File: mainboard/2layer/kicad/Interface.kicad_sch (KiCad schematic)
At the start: 61 parts, among them J1 Conn_02x10_Odd_Even_MountingP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, J21 Conn_01x01_Male, J22 Conn_01x01_Male, J3 DIN-5, J4 DIN-5, J6 Conn_01x10, P11 1N4148, P12 1N4148, P13 1N4148, P14 1N4148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

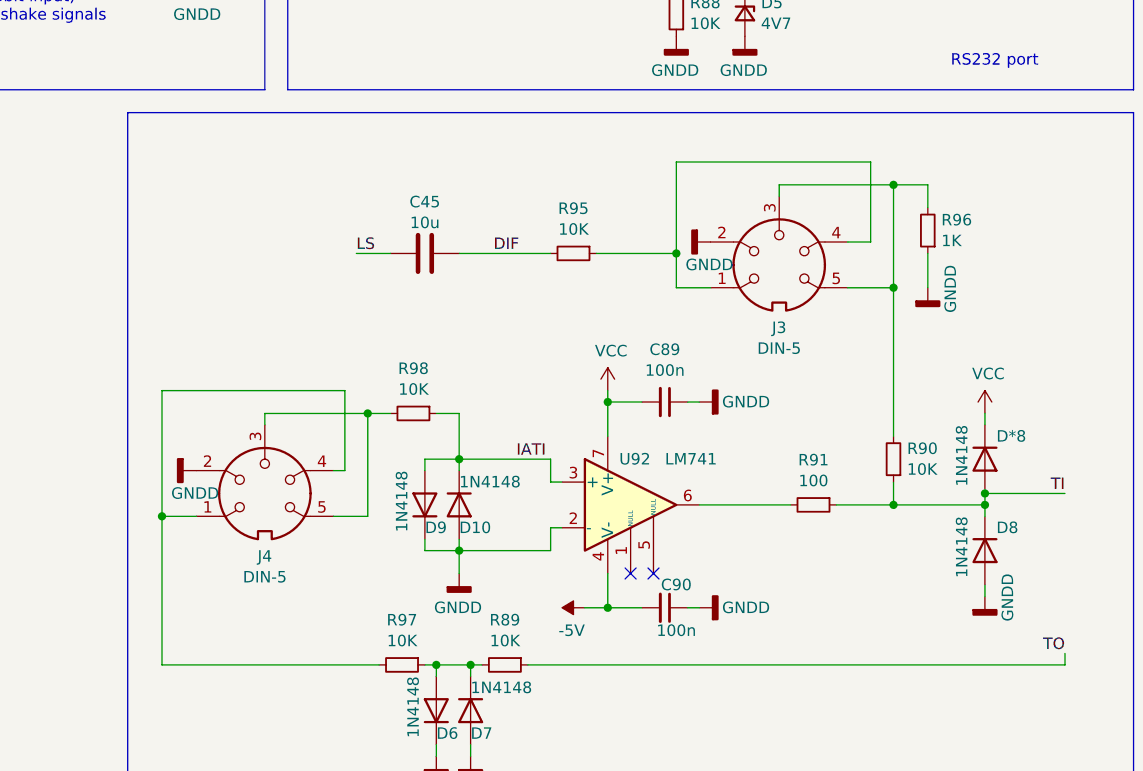
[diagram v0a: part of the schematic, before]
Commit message: Fixes for PCB DRC: trace clearance, footprints, board edges
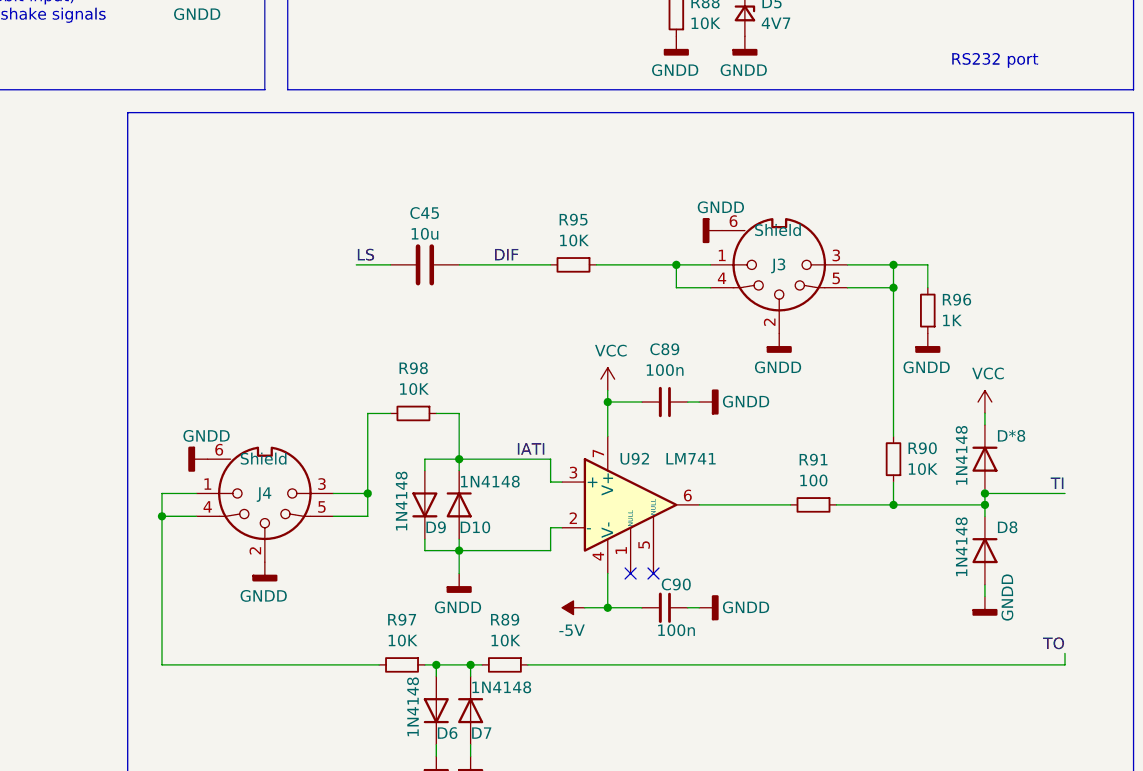
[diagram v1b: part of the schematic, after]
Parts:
- removed J3: DIN-5, Connectors_UNITRA:DIN-5, symbol Connector:DIN-5
- removed J4: DIN-5, Conectors_Unitra:DIN-5, symbol Connector:DIN-5
- added J3, J4: DIN-5, Cobra_original:DIN-5, symbol Connector:DIN-5_180degree_GND
- D*8, D10, D5, D6, D7, D8, D9, P11, P12, P13, P14, P15, P16, P17, P18: footprint Diode_THT:D_DO-35_SOD27_P7.62mm_Horizontal -> Cobra_original:D_DO-35_SOD27_P7.62mm_Horizontal
- J6, JA5, JB5: footprint Connector_PinHeader_2.54mm:PinHeader_1x10_P2.54mm_Vertical -> Cobra_original:PinHeader_1x10_P2.54mm_Vertical
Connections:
- net GNDD: now also J3.2, J3.6 (Shield), J4.2, J4.6 (Shield)
- net at R97.2: now also J4.1, J4.4
- net at R90.2, R96.2: now also J3.3, J3.5
- net at R98.2: now also J4.3, J4.5
- net at R95.1: now also J3.1, J3.4
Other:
- moved on the sheet: C45, R95, R96
